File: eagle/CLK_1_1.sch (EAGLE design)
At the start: 20 parts, among them IC1 4521N, Q1 4.194304MHz, X1 Out Ctrl, X2 IO Ctrl

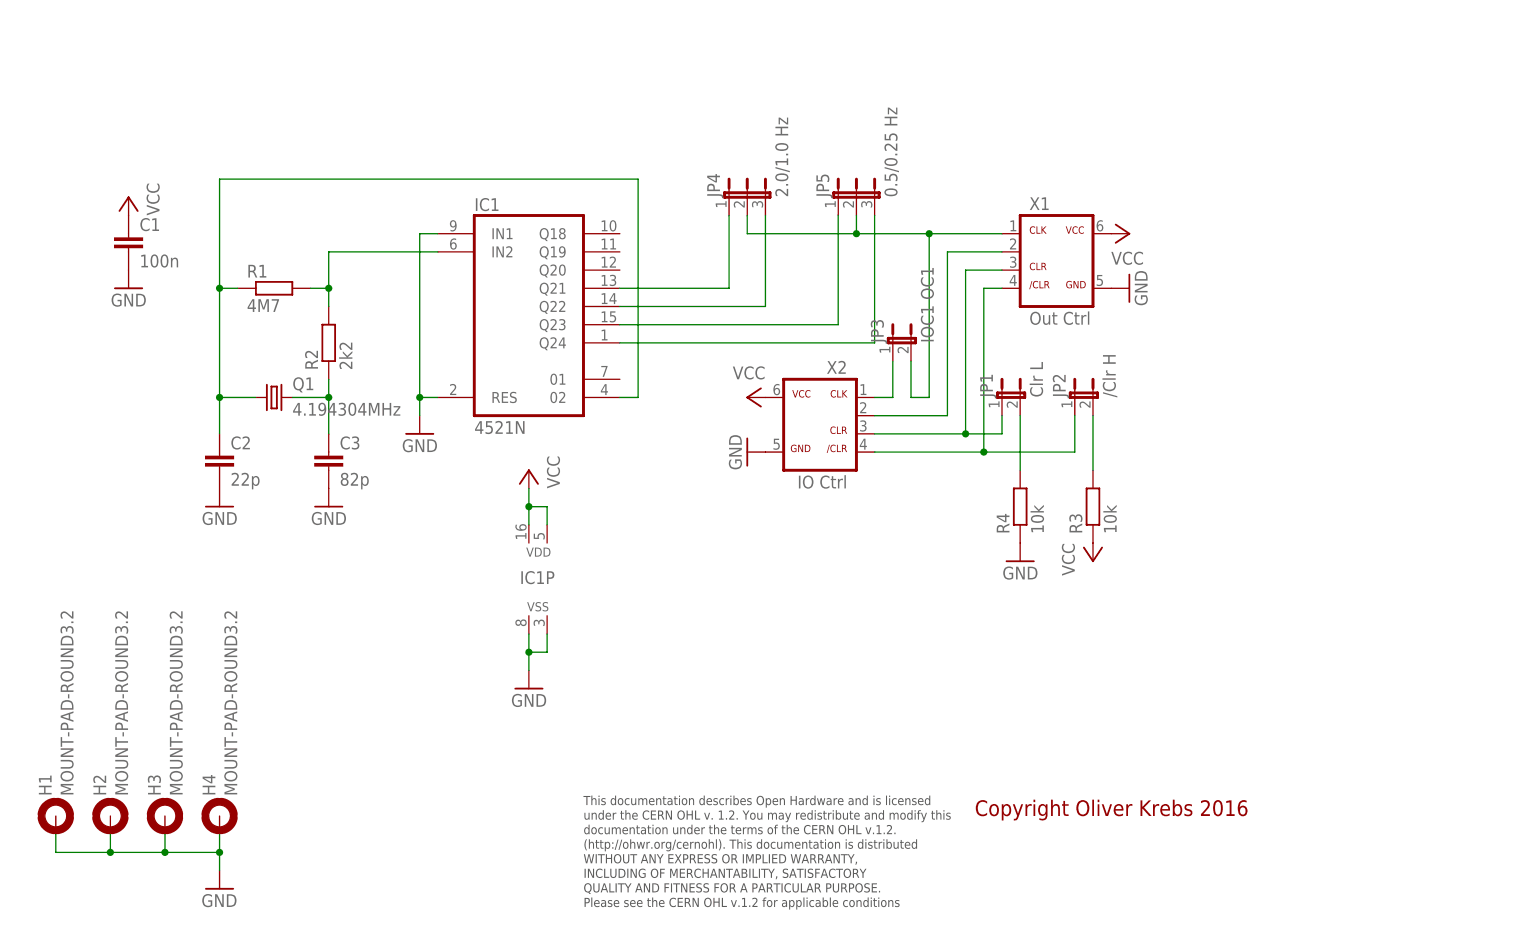
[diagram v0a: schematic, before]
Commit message: Add new tetra-Board and arduino files
Add AMP_1_0, AVC_1_0, D18_1_1, IOP_1_2, MIC_1_0, PIN_1_1, POT_1_0, PWA_1_0, PWR_1_0, RGF 2.0, SOC_2_0, VLT_1_0
Add mex_nano_shield_keyboard, mex_nano_shied_numbers

New arduino projects
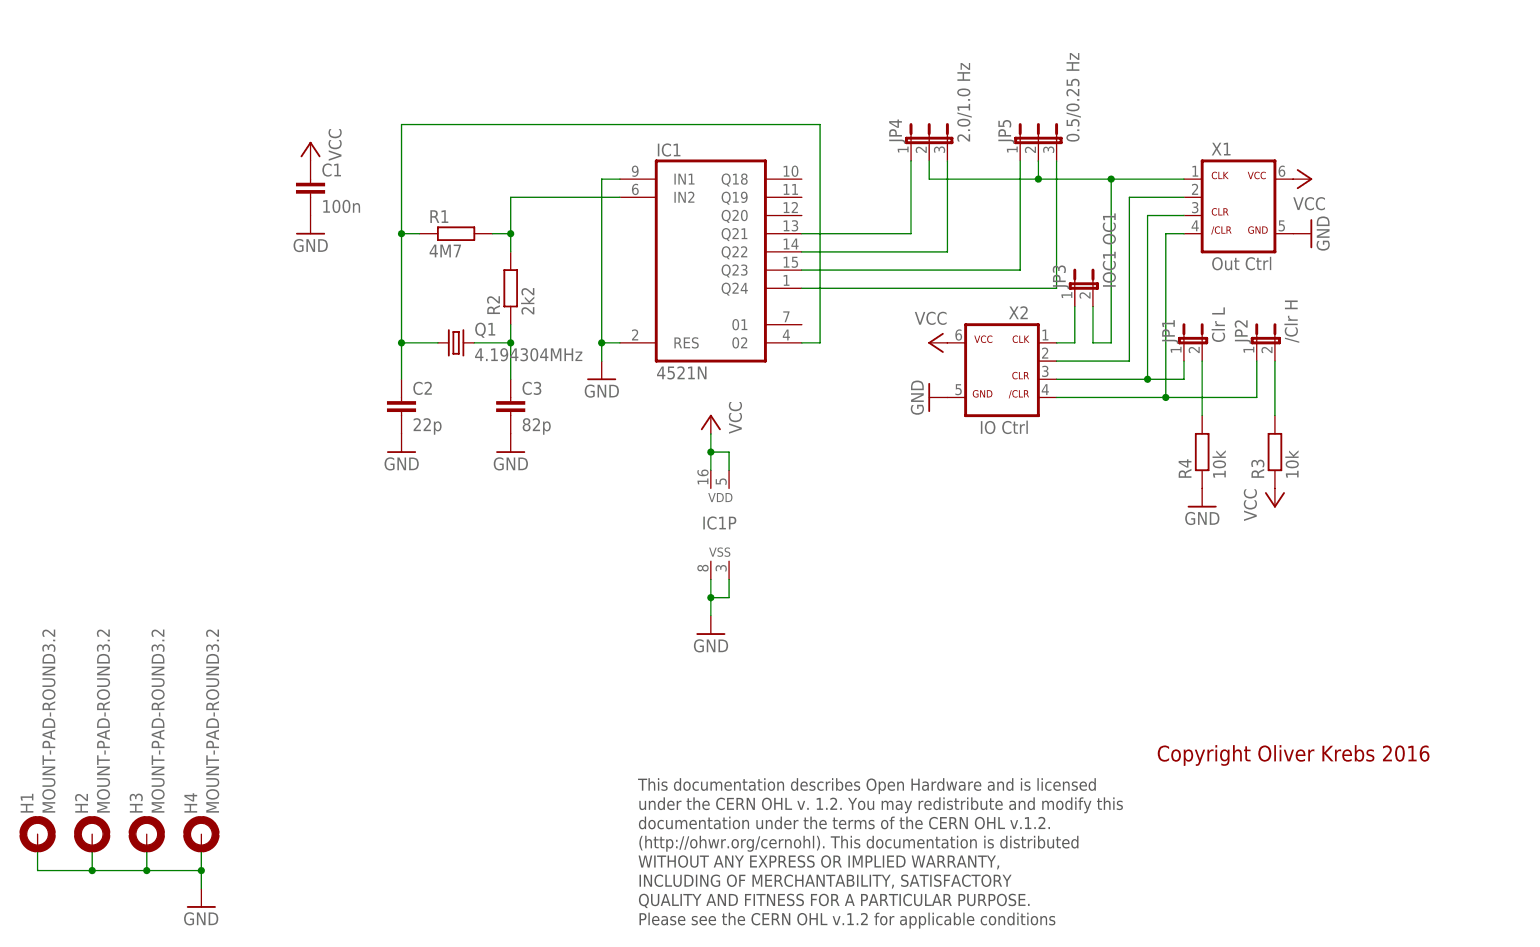
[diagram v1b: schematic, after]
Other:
- moved on the sheet: C1, C2, C3, H1, H2, H3, H4, IC1, IC1P, JP1, JP2, JP3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
